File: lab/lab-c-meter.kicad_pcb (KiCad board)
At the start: 2 copper layers, 41.9 x 25.4 mm, 20 parts, among them J1 IN, U1 LM324

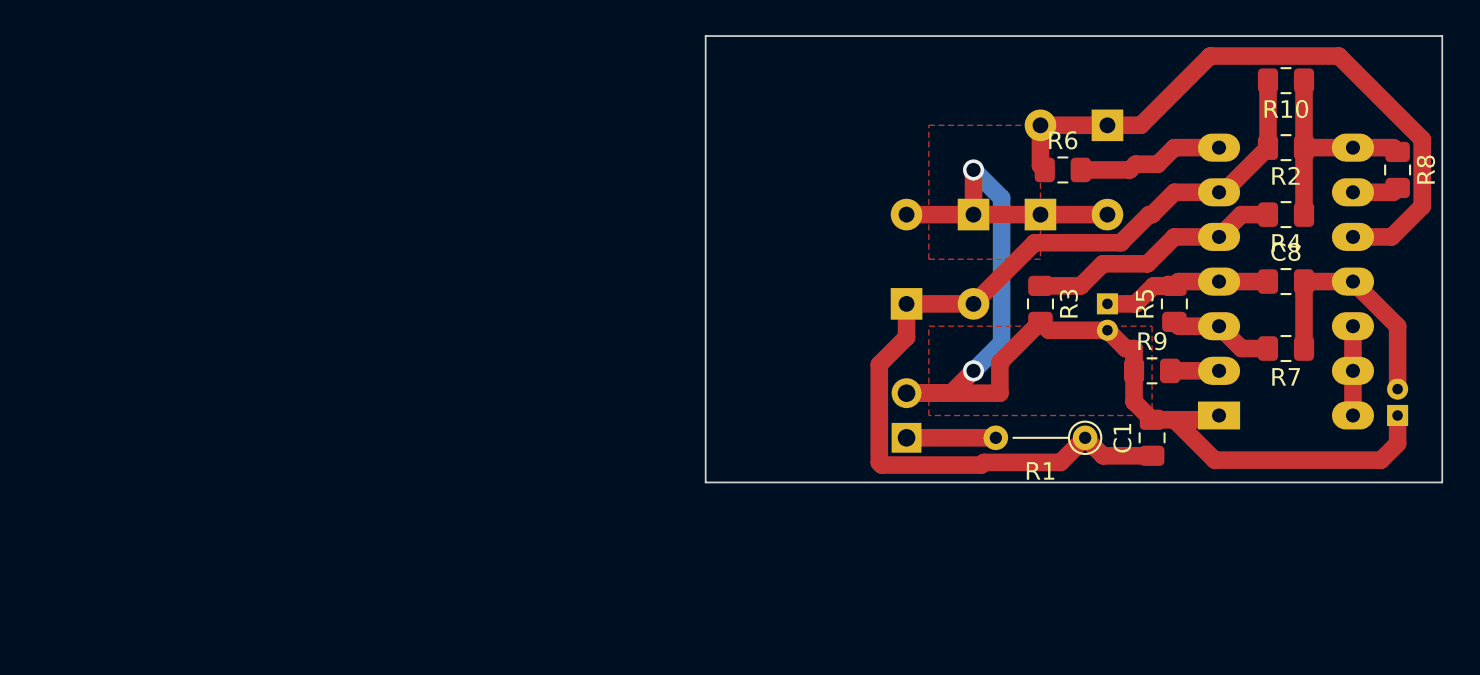
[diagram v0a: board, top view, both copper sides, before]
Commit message: Added elements to PCB
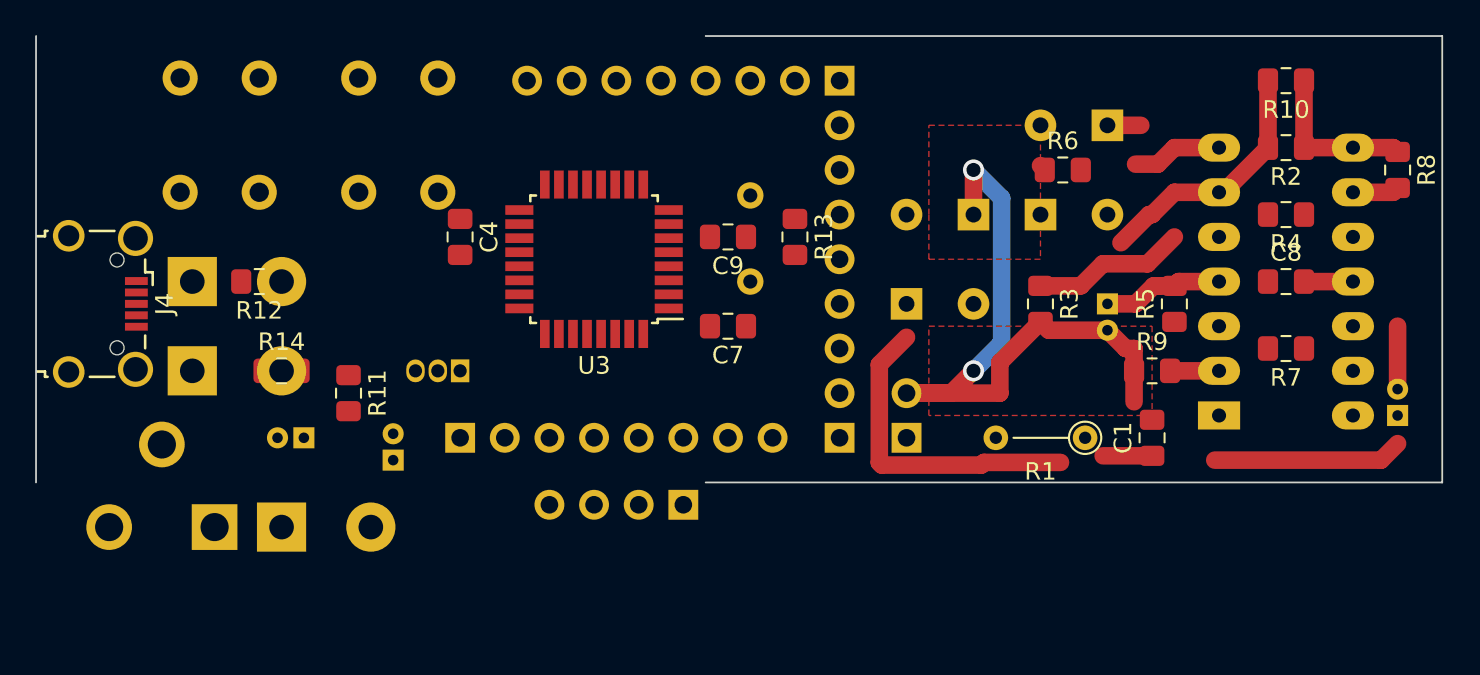
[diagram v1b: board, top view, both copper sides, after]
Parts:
- added C4: 100n, Capacitor_SMD:C_0805_2012Metric_Pad1.15x1.40mm_HandSolder, F.Cu at (43.2, 40.6)
- added C5: 4u7 6.3V, Capacitor_THT:CP_Radial_D4.0mm_P1.50mm, B.Cu at (34.3, 52.1)
- added C6: 4u7 6.3V, Capacitor_THT:CP_Radial_D4.0mm_P1.50mm, B.Cu at (39.4, 53.3)
- added C7: 22p, Capacitor_SMD:C_0805_2012Metric_Pad1.15x1.40mm_HandSolder, F.Cu at (58.4, 45.7)
- added C9: 22p, Capacitor_SMD:C_0805_2012Metric_Pad1.15x1.40mm_HandSolder, F.Cu at (58.4, 40.6)
- added D5: M7, Diode_THT:D_5W_P5.08mm_Vertical_AnodeUp, B.Cu at (33.0, 57.1)
- added D6: 3v6, Diode_THT:D_5W_P5.08mm_Vertical_KathodeUp, B.Cu at (27.9, 43.2)
- added D7: 3v6, Diode_THT:D_5W_P5.08mm_Vertical_KathodeUp, B.Cu at (27.9, 48.3)
- added J2: Barrel_Jack_Switch, Connector_BarrelJack:BarrelJack_CUI_PJ-102AH_Horizontal, B.Cu at (29.2, 57.1)
- added J3: Conn_01x04, Connector_PinHeader_2.54mm:PinHeader_1x04_P2.54mm_Vertical, B.Cu at (55.9, 55.9)
- added J4: USB_B_Mini, Connector_USB:USB_Micro-B_Wuerth_629105150521_CircularHoles, F.Cu at (22.9, 44.5)
- added J5: PB, Connector_PinHeader_2.54mm:PinHeader_1x08_P2.54mm_Vertical, B.Cu at (64.8, 31.8)
- added J6: PC, Connector_PinHeader_2.54mm:PinHeader_1x08_P2.54mm_Vertical, B.Cu at (43.2, 52.1)
- added J7: PD, Connector_PinHeader_2.54mm:PinHeader_1x08_P2.54mm_Vertical, B.Cu at (64.8, 52.1)
- added R11: 1k5, Resistor_SMD:R_0805_2012Metric_Pad1.15x1.40mm_HandSolder, F.Cu at (36.8, 49.5)
- added R12: 68R, Resistor_SMD:R_0805_2012Metric_Pad1.15x1.40mm_HandSolder, F.Cu at (31.8, 43.2)
- added R13: 1M, Resistor_SMD:R_0805_2012Metric_Pad1.15x1.40mm_HandSolder, F.Cu at (62.2, 40.6)
- added R14: 68R, Resistor_SMD:R_0805_2012Metric_Pad1.15x1.40mm_HandSolder, F.Cu at (33.0, 48.3)
- added SW1: SW_Push, Button_Switch_THT:SW_PUSH_6mm_H4.3mm, B.Cu at (41.9, 38.1)
- added SW2: SW_Push, Button_Switch_THT:SW_PUSH_6mm_H4.3mm, B.Cu at (31.8, 38.1)
- added U2: L7805, Package_TO_SOT_THT:TO-92S, B.Cu at (43.2, 48.3)
- added U3: ATmega8-16AU, Package_QFP:TQFP-32_7x7mm_P0.8mm, F.Cu at (50.8, 41.9)
- added Y1: 16MHz, Crystal:Crystal_HC18-U_Vertical, B.Cu at (59.7, 43.2)
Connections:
- net CON renamed CNT
- net GNDD renamed GND
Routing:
- net Net-(D3-Pad1): track 36.4 -> 2.25 mm
- net MID: track 71.4 -> 50.1 mm
- net Net-(C1-Pad1): track 54.4 -> 35.4 mm
- net GND: track 13.8 -> 6.37 mm
- net Net-(R5-Pad1): track 5.95 -> 0.00 mm
- net Net-(R3-Pad1): track 14.6 -> 8.77 mm
- net Net-(J1-Pad1): track 5.08 -> 0.00 mm
- net (no net): track 5.08 -> 0.00 mm
- net Net-(R10-Pad1): track 13.0 -> 9.24 mm
- net CNT: track 8.39 -> 5.14 mm
- net +5V: track 9.66 -> 6.88 mm
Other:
- board size 41.9 x 25.4 mm -> 80 x 25.4 mm

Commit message: Expanded the PCB
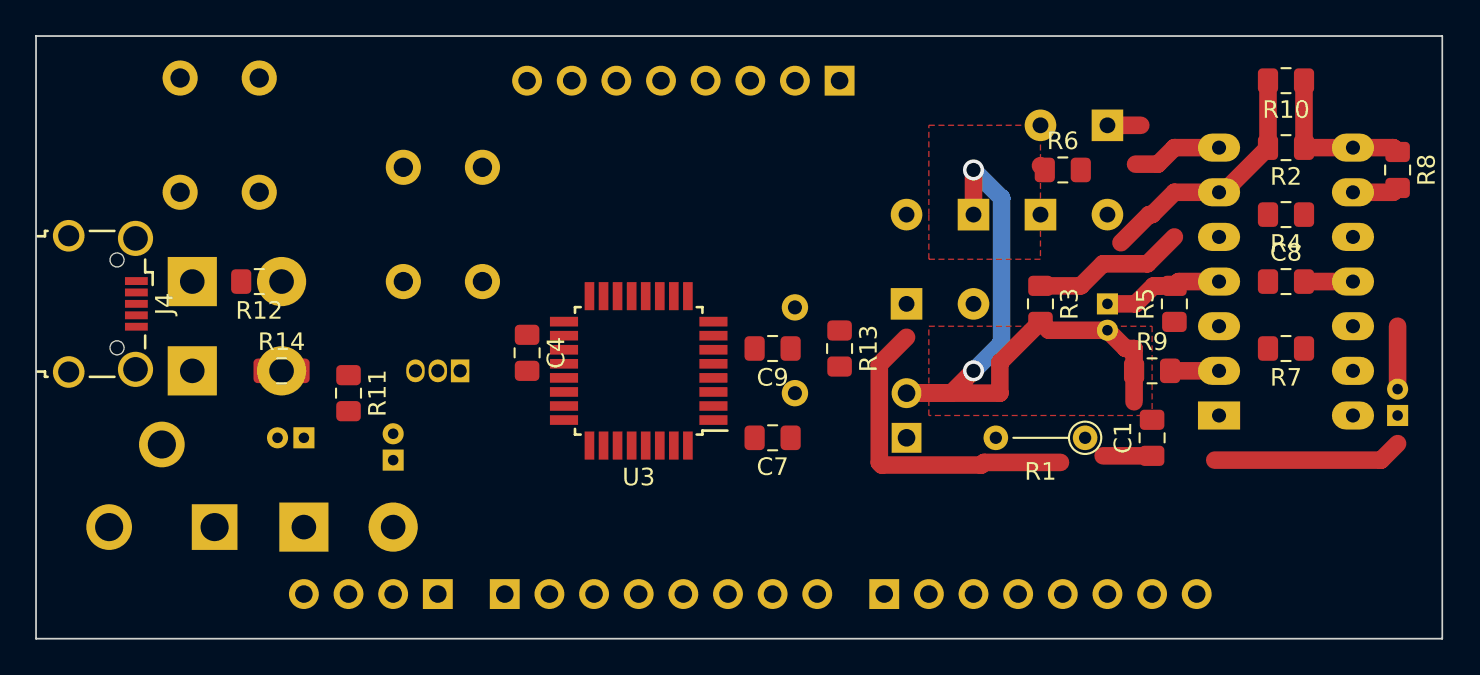
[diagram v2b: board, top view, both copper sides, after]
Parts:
- SW1, SW2: footprint Button_Switch_THT:SW_PUSH_6mm_H4.3mm -> Button_Switch_THT:SW_PUSH_6mm
- Y1: footprint Crystal:Crystal_HC18-U_Vertical -> Crystal:Crystal_HC49-U_Vertical
- moved J3 14.9 mm to (41.9, 61.0)
- moved J7 9.25 mm to (67.3, 61.0), turned to 270 degrees
- moved J6 9.25 mm to (45.7, 61.0)
- moved C4 7.62 mm to (47.0, 47.2)
- moved U3 6.84 mm to (53.3, 48.3)
- moved C7 6.84 mm to (61.0, 52.1)
- moved C9 6.84 mm to (61.0, 47.0)
- moved R13 6.84 mm to (64.8, 47.0)
- moved Y1 6.84 mm to (62.2, 49.5)
- moved SW1 5.68 mm to (44.5, 43.2)
- moved D5 1.27 mm to (34.3, 57.1)
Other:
- board size 80 x 25.4 mm -> 80 x 34.3 mm

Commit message: Finished
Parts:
- R1: moved to B.Cu
- moved C8 63.5 mm to (27.3, 52.4), turned to 270 degrees
- moved J4 46.6 mm to (66.9, 59.8), turned to 0 degrees
- moved D7 41.9 mm to (69.8, 49.5), turned to 90 degrees
- moved D6 35.5 mm to (61.8, 53.7)
- moved R12 31.1 mm to (59.5, 57.1), turned to 0 degrees
- moved J1 30.7 mm to (92.7, 33.0), turned to 90 degrees
- moved R14 30.1 mm to (63.1, 50.2)
- moved R11 29.6 mm to (66.4, 48.4), turned to 90 degrees
- moved C5 27.0 mm to (60.4, 45.3), turned to 90 degrees
- moved D1 24.1 mm to (90.2, 55.2)
- moved C3 24.1 mm to (72.6, 53.6), turned to 180 degrees
- moved D3 23.6 mm to (79.3, 57.9), turned to 180 degrees
- moved D2 23.6 mm to (93.3, 50.2)
- moved J3 22.5 mm to (21.8, 50.8), turned to 180 degrees
- moved R6 22.2 mm to (83.1, 58.3)
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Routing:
- net GND: track 6.37 -> 237.9 mm, vias 0 -> 3
- net +5V: track 6.88 -> 182.0 mm, vias 0 -> 5
- net CNT: track 5.14 -> 57.2 mm, vias 0 -> 2
- net PD7: track 0.00 -> 43.8 mm
- net Net-(SW1-Pad2): track 0.00 -> 39.2 mm, vias 0 -> 2
- net MID: track 50.1 -> 87.6 mm, vias 2 -> 0
- net VIN: track 0.00 -> 36.9 mm
- net ADC6: track 0.00 -> 35.8 mm, vias 0 -> 2
- net ADC7: track 0.00 -> 35.3 mm, vias 0 -> 2
- net Net-(D3-Pad1): track 2.25 -> 31.5 mm
- net Net-(D7-Pad1): track 0.00 -> 29.2 mm
- net D-: track 0.00 -> 26.5 mm
- net D+: track 0.00 -> 23.6 mm
- net PD0: track 0.00 -> 22.7 mm
- net PD1: track 0.00 -> 22.3 mm
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- added copper zone on F.Cu, net +5V
- added copper zone on F.Cu, net CNT
- added copper zone on F.Cu, net GND
- added copper zone on F.Cu, net Net-(R5-Pad1)
- removed copper zone on F.Cu, net MID
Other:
- board text added: "C-METHER V 1.0"
- board text added: "iscnet.ru"

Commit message: Production
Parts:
- D6: footprint Diode_THT:D_5W_P5.08mm_Vertical_KathodeUp -> Diode_THT:D_A-405_P2.54mm_Vertical_AnodeUp
- D7: footprint Diode_THT:D_5W_P5.08mm_Vertical_KathodeUp -> Diode_THT:D_A-405_P2.54mm_Vertical_KathodeUp
- J2: footprint Connector_BarrelJack:BarrelJack_CUI_PJ-102AH_Horizontal -> local:Barrel-little-11mm-x-5mm; moved to F.Cu
- J4: footprint Connector_USB:USB_Micro-B_Wuerth_629105150521_CircularHoles -> local:USB-mini-S2126.12010-Circular; moved to B.Cu
- R1: footprint Resistor_THT:R_Axial_DIN0204_L3.6mm_D1.6mm_P5.08mm_Vertical -> Resistor_THT:R_Axial_DIN0414_L11.9mm_D4.5mm_P15.24mm_Horizontal
- U2: value L7805 -> L78L05_TO92; footprint Package_TO_SOT_THT:TO-92S -> Package_TO_SOT_THT:TO-92_HandSolder
- moved R1 9.86 mm to (96.5, 51.4)
- moved J2 6.19 mm to (25.5, 31.1), turned to 0 degrees
- moved C1 6.15 mm to (95.2, 45.7), turned to 90 degrees
- moved J4 5.29 mm to (67.1, 54.5), turned to 180 degrees
- moved D1 5.08 mm to (90.2, 60.3)
- moved D2 5.08 mm to (93.3, 55.2)
- moved U2 2.49 mm to (27.2, 57.8), turned to 270 degrees
- moved R6 1.92 mm to (83.2, 60.2)
- moved D6 1.33 mm to (63.1, 53.8)
- moved C3 0.76 mm to (72.6, 52.8)
- moved R14 0.70 mm to (63.0, 49.5)
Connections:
- U2 pad 1: VIN -> +5V
- U2 pad 3: +5V -> VIN
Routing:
- net +5V: track 182.0 -> 203.2 mm
- net Net-(J5-Pad1): track 15.7 -> 26.4 mm, vias 0 -> 2
- net Net-(J5-Pad3): track 11.0 -> 19.6 mm, vias 0 -> 2
- net PD7: track 43.8 -> 38.6 mm
- net VIN: track 36.9 -> 31.8 mm
- net MID: track 87.6 -> 82.6 mm
- net Net-(C1-Pad1): track 37.6 -> 42.5 mm
- net ADC7: track 35.3 -> 31.1 mm
- net ADC6: track 35.8 -> 40.0 mm
- net PC5: track 15.7 -> 11.6 mm
- net CNT: track 57.2 -> 61.0 mm
- net PD1: track 22.3 -> 18.8 mm
- net Net-(R10-Pad1): track 12.7 -> 15.2 mm
- net Net-(D3-Pad1): track 31.5 -> 29.2 mm
- net PD4: track 19.7 -> 21.9 mm
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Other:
- net class Default: via_dia 1.2 -> 1; via_drill 0.8 -> 0.6
- net class mid: via_dia 1.2 -> 1; via_drill 0.8 -> 0.6
- net class wide: via_dia 1.2 -> 1; via_drill 0.8 -> 0.6

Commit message: Shifted top level for buttons.
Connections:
- net Net-(J5-Pad3) renamed SS
- net Net-(J5-Pad4) renamed MOSI
- net Net-(J5-Pad5) renamed MISO
- net Net-(J5-Pad6) renamed SCK
- net Net-(SW1-Pad2) renamed ~RESET
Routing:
- net GND: track 237.0 -> 235.9 mm

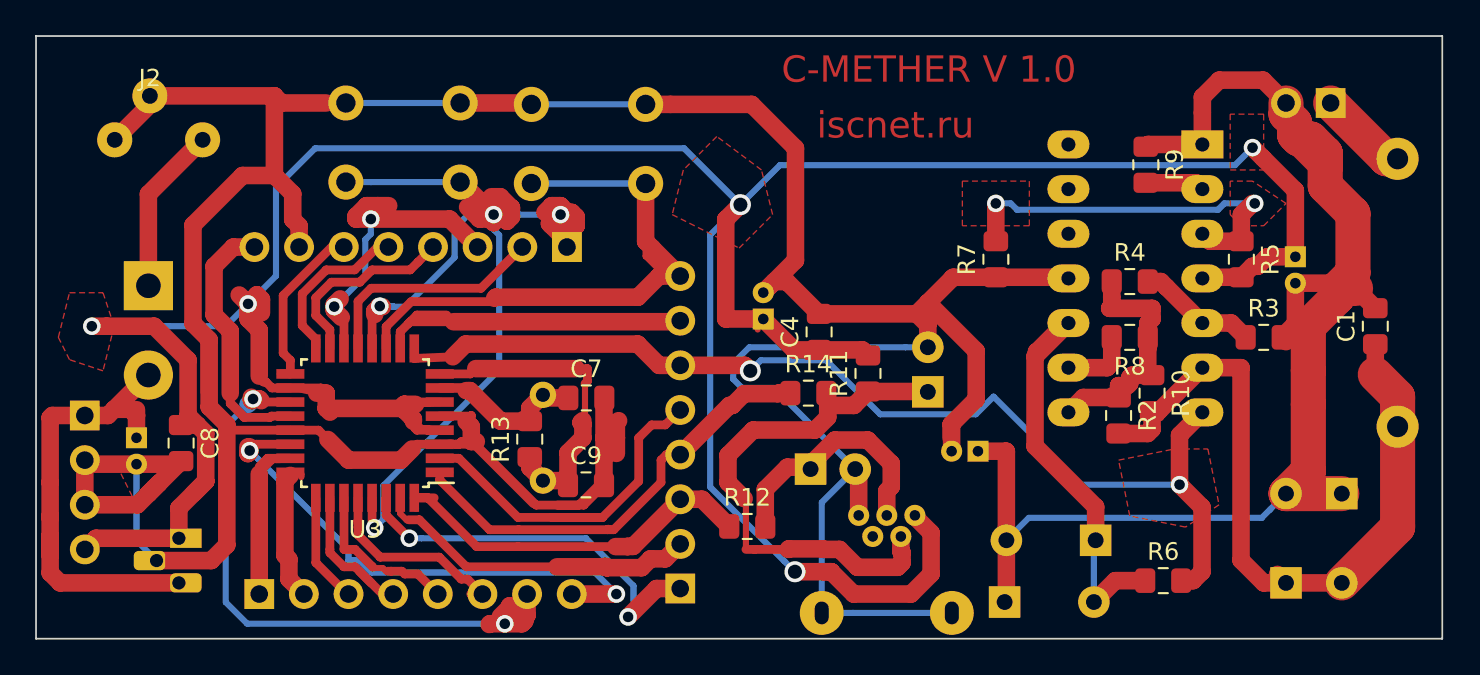
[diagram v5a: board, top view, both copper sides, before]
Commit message: Corrected HW errors.
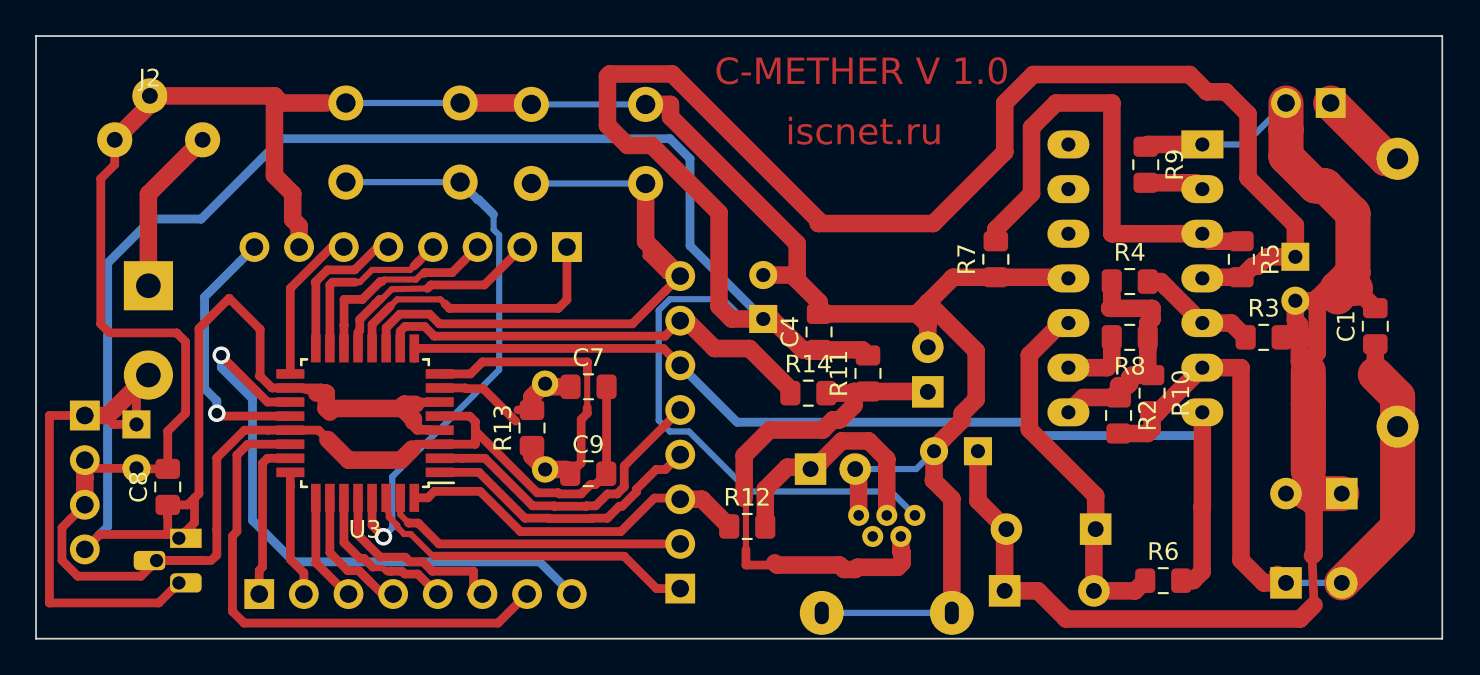
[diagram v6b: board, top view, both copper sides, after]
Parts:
- C2, C3, C5, C6: footprint Capacitor_THT:CP_Radial_D4.0mm_P1.50mm -> Capacitor_THT:CP_Radial_D5.0mm_P2.50mm
- SW1: value SW_Push -> RST
- SW2: value SW_Push -> BLD
- moved C8 2.61 mm to (26.5, 54.9), turned to 90 degrees
- moved C6 0.76 mm to (24.8, 51.3)
- moved C7 0.65 mm to (50.5, 49.2)
- moved C9 0.65 mm to (50.5, 54.1)
- moved R13 0.65 mm to (47.3, 51.5)
- moved Y1 0.65 mm to (48.0, 49.0)
- moved D3 0.63 mm to (79.3, 57.3)
- moved D4 0.63 mm to (74.2, 60.8)
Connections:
- J6 pad 7: ADC6 -> ADC7
- J6 pad 8: ADC7 -> ADC6
- J7 pad 4: D- -> PD3
- J7 pad 7: PD6 -> D-
- U3 pad 1: D- -> PD3
- U3 pad 10: PD6 -> D-
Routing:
- net GND: track 235.9 -> 202.4 mm
- net +5V: track 203.2 -> 236.5 mm, vias 5 -> 0
- net PD6: track 19.5 -> 0.00 mm
- net PD3: track 0.00 -> 16.4 mm
- net Net-(J5-Pad1): track 26.4 -> 16.5 mm, vias 2 -> 0
- net SS: track 19.6 -> 11.7 mm, vias 2 -> 0
- net Net-(D3-Pad1): track 29.2 -> 21.3 mm
- net Net-(C7-Pad1): track 15.6 -> 9.22 mm
- net Net-(R5-Pad1): track 22.3 -> 27.8 mm, vias 2 -> 0
- net ADC6: track 40.0 -> 35.1 mm, vias 2 -> 1
- net ~RESET: track 37.3 -> 32.8 mm, vias 2 -> 1
- net PD4: track 21.9 -> 17.8 mm
- net PD0: track 23.4 -> 19.5 mm, vias 2 -> 0
- net AREF: track 18.4 -> 15.2 mm, vias 0 -> 1
- net D+: track 23.6 -> 21.1 mm
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- removed copper zone on F.Cu, net +5V
- removed copper zone on F.Cu, net CNT
- removed copper zone on F.Cu, net GND
- removed copper zone on F.Cu, net Net-(R5-Pad1)

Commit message: Added AO book and AC Voltage detector.
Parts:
- added C10: 100n, Capacitor_SMD:C_0805_2012Metric_Pad1.15x1.40mm_HandSolder, F.Cu at (66.4, 39.4)
- added D8: 4148, Diode_THT:D_A-405_P5.08mm_Vertical_KathodeUp, F.Cu at (70.1, 31.2)
- added D9: LED, LED_THT:LED_D3.0mm, F.Cu at (84.3, 31.6)
- added R15: 10k, Resistor_SMD:R_0805_2012Metric_Pad1.15x1.40mm_HandSolder, F.Cu at (72.9, 39.6)
- added R16: 4K7, Resistor_SMD:R_0805_2012Metric_Pad1.15x1.40mm_HandSolder, F.Cu at (80.6, 39.4)
- added R17: 10R, Resistor_SMD:R_0805_2012Metric_Pad1.15x1.40mm_HandSolder, F.Cu at (87.1, 31.5)
- moved R7 1.78 mm to (73.5, 43.7)
- moved R9 0.76 mm to (82.4, 35.8)
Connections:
- U1 pad 12: (no net) -> Net-(R16-Pad2)
- U1 pad 13: (no net) -> Net-(D8-Pad2)
- U1 pad 14: (no net) -> Net-(D8-Pad1)
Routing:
- net CNT: track 60.0 -> 105.9 mm, vias 0 -> 1
- net +5V: track 236.5 -> 193.6 mm
- net Net-(D8-Pad1): track 0.00 -> 15.6 mm
- net Net-(R5-Pad1): track 27.8 -> 15.6 mm
- net Net-(D8-Pad2): track 0.00 -> 11.4 mm
- net MID: track 82.9 -> 93.7 mm
- net Net-(C10-Pad1): track 0.00 -> 4.53 mm
- net Net-(D9-Pad1): track 0.00 -> 3.27 mm
- net Net-(R16-Pad2): track 0.00 -> 2.28 mm
- net GND: track 202.4 -> 200.3 mm
- net Net-(R9-Pad2): track 3.37 -> 3.94 mm
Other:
- board text removed: "C-METHER V 1.0"
- board text removed: "iscnet.ru"

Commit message: Make vias bigger.
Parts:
- added JP1: WATCH, Connector_PinHeader_2.54mm:PinHeader_1x02_P2.54mm_Vertical, F.Cu at (62.7, 35.1)
- D9: value LED -> AC
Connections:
- C10 pad 2: CNT -> Net-(C10-Pad2)
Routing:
- net CNT: track 105.9 -> 111.3 mm, vias 1 -> 0
- net Net-(C10-Pad2): track 0.00 -> 4.37 mm
- net ADC6: track 35.1 -> 35.9 mm
- net +5V: track 193.6 -> 194.3 mm
- net AREF: track 15.2 -> 14.5 mm
- net GND: track 200.3 -> 200.9 mm
- net PC5: track 12.3 -> 12.9 mm
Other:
- net class Default: via_dia 1 -> 1.5
- net class mid: via_dia 1 -> 1.5
- net class wide: via_dia 1 -> 1.5
